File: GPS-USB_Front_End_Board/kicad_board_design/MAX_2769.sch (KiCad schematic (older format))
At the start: 50 parts, among them J3 SMA, P2 CONN_01X03, U4 MAX8510, U5 MAX8510, U6 MAX2771, U7 SAWTEK-855969, U8 LT1719S6 -- Not Populated, X1 13.368MHz TCXO

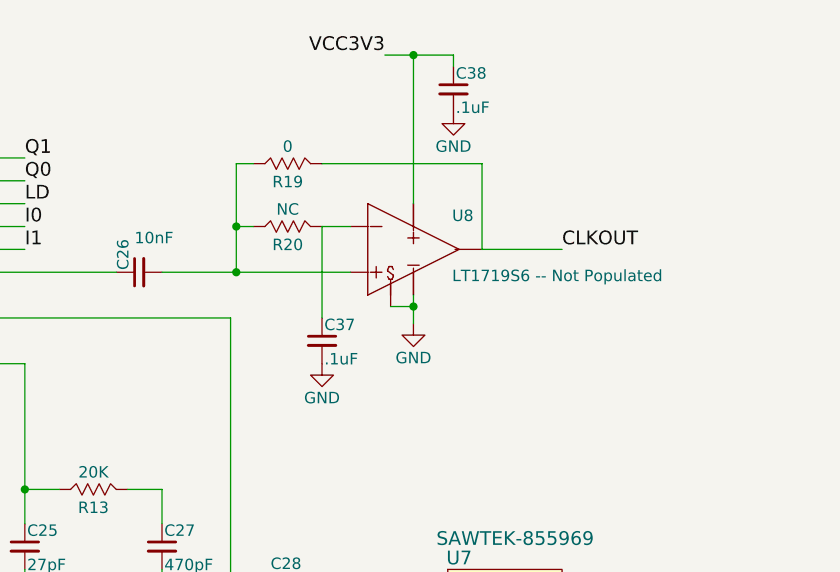
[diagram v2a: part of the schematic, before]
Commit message: Moved optional Maxim clk fix circuit to FTDI side.
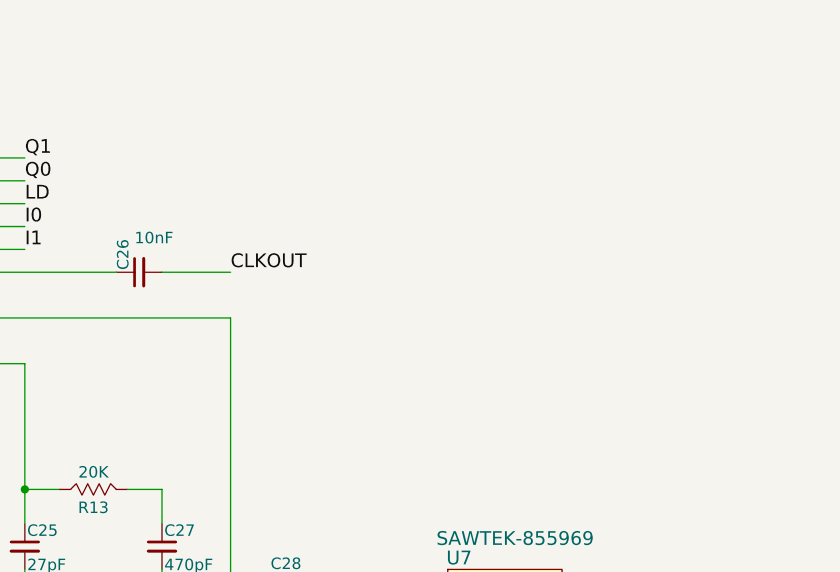
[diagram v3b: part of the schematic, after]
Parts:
- removed C37, C38: .1uF, Capacitors_SMD:C_0402, symbol C_Small
- removed R19: 0, Resistors_SMD:R_0603_HandSoldering, symbol R
- removed R20: NC, Resistors_SMD:R_0603_HandSoldering, symbol R
- removed U8: LT1719S6 -- Not Populated, rf:TSOT-23_S6, symbol LT1719S6
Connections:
- net CLKOUT: now also C26.2
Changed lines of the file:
@@
 	0    1    1    0
-$EndComp
-$Comp
-L LT1719S6 U8
-U 1 1 5B5E9B54
-P 9375 1250
-F 0 "U8" H 9544 968 50  0000 L BNN
-F 1 "LT1719S6 -- Not Populated" H 9544 705 50  0000 L BNN
-F 2 "rf:TSOT-23_S6" H 9375 1250 60  0001 C CNN
-F 3 "Unavailable" H 9375 1250 50  0001 L BNN
-F 4 "LT1719" H 9375 1250 50  0001 L BNN "Field4"
-F 5 "None" H 9375 1250 50  0001 L BNN "Field5"
-F 6 "Analog Devices / Linear Technology" H 9375 1250 50  0001 L BNN "Field6"
-F 7 "None" H 9375 1250 50  0001 L BNN "Field7"
-F 8 "Linear Tech" H 0   0   50  0001 C CNN "MFR"
-F 9 "LT1719IS6#TRMPBF" H 0   0   50  0001 C CNN "MPN"
-F 10 "Digikey" H 0   0   50  0001 C CNN "SPR"
-F 11 "LT1719IS6#TRMPBFCT-ND" H 0   0   50  0001 C CNN "SPN"
-F 12 "-" H 0   0   50  0001 C CNN "SPURL"
-	1    9375 1250
-	1    0    0    -1
-$EndComp
-$Comp
-L R R20
-U 1 1 5B5E9ED0
-P 8825 1550
-F 0 "R20" V 8905 1550 50  0000 C CNN
-F 1 "NC" V 8750 1550 50  0000 C CNN
-F 2 "Resistors_SMD:R_0603_HandSoldering" V 8680 1550 50  0001 C CNN
-F 3 "" H 8750 1550 50  0001 C CNN
-F 4 "Vishay" H 0   0   50  0001 C CNN "MFR"
-F 5 "CRCW06030000Z0EBC" H 0   0   50  0001 C CNN "MPN"
-F 6 "Digikey" H 0   0   50  0001 C CNN "SPR"
-F 7 "541-4013-1-ND" H 0   0   50  0001 C CNN "SPN"
-F 8 "-" H 0   0   50  0001 C CNN "SPURL"
-	1    8825 1550
-	0    1    1    0
-$EndComp
-$Comp
-L GND #PWR040
-U 1 1 5B5EA299
-P 8975 2150
-F 0 "#PWR040" H 8975 1900 50  0001 C CNN
-F 1 "GND" H 8975 2000 50  0000 C CNN
-F 2 "" H 8975 2150 50  0000 C CNN
-F 3 "" H 8975 2150 50  0000 C CNN
-	1    8975 2150
-	1    0    0    -1
-$EndComp
-$Comp
-L GND #PWR041
-U 1 1 5B5EAC9C
-P 9375 1975
-F 0 "#PWR041" H 9375 1725 50  0001 C CNN
-F 1 "GND" H 9375 1825 50  0000 C CNN
-F 2 "" H 9375 1975 50  0000 C CNN
-F 3 "" H 9375 1975 50  0000 C CNN
-	1    9375 1975
-	1    0    0    -1
-$EndComp
-$Comp
-L R R19
-U 1 1 5B5EB863
-P 8825 1275
-F 0 "R19" V 8905 1275 50  0000 C CNN
-F 1 "0" V 8750 1275 50  0000 C CNN
-F 2 "Resistors_SMD:R_0603_HandSoldering" V 8680 1275 50  0001 C CNN
-F 3 "" H 8750 1275 50  0001 C CNN
-F 4 "Vishay" H 0   0   50  0001 C CNN "MFR"
-F 5 "CRCW06030000Z0EBC" H 0   0   50  0001 C CNN "MPN"
-F 6 "Digikey" H 0   0   50  0001 C CNN "SPR"
-F 7 "541-4013-1-ND" H 0   0   50  0001 C CNN "SPN"
-F 8 "-" H 0   0   50  0001 C CNN "SPURL"
-	1    8825 1275
-	0    1    1    0
-$EndComp
-$Comp
-L C_Small C38
-U 1 1 5B5EE1F7
-P 9550 950
-F 0 "C38" H 9560 1020 50  0000 L CNN
-F 1 ".1uF" H 9560 870 50  0000 L CNN
-F 2 "Capacitors_SMD:C_0402" H 9550 950 50  0001 C CNN
-F 3 "" H 9550 950 50  0001 C CNN
-F 4 "TDK" H 0   0   50  0001 C CNN "MFR"
-F 5 "CGA2B1X7R1C104K050BC" H 0   0   50  0001 C CNN "MPN"
-F 6 "Digikey" H 0   0   50  0001 C CNN "SPR"
-F 7 "445-5613-1-ND" H 0   0   50  0001 C CNN "SPN"
-F 8 "-" H 0   0   50  0001 C CNN "SPURL"
-	1    9550 950
-	1    0    0    -1
-$EndComp
-$Comp
-L GND #PWR042
-U 1 1 5B5EE330
-P 9550 1050
-F 0 "#PWR042" H 9550 800 50  0001 C CNN
-F 1 "GND" H 9550 900 50  0000 C CNN
-F 2 "" H 9550 1050 50  0000 C CNN
-F 3 "" H 9550 1050 50  0000 C CNN
-	1    9550 1050
-	1    0    0    -1
 $EndComp
 Text Label 3100 2650 2    60   ~ 0
@@
 Text Label 7675 1650 0    60   ~ 0
 I1
-Text Label 10025 1650 0    60   ~ 0
+Text Label 8575 1750 0    60   ~ 0
 CLKOUT
 Text Label 2175 2650 0    60   ~ 0
@@
 Text Label 1850 1650 0    60   ~ 0
 VCC3V3
-Text Label 9250 800  2    60   ~ 0
-VCC3V3
 Text Label 1825 4375 0    60   ~ 0
 +5V
@@
 	7475 1650 7675 1650
 Wire Wire Line
-	8275 1750 9100 1750
-Wire Wire Line
 	1400 2650 1775 2650
 Wire Wire Line
@@
 Wire Wire Line
 	8575 3150 8725 3150
-Wire Wire Line
-	9100 1550 8975 1550
-Wire Wire Line
-	8675 1550 8600 1550
-Wire Wire Line
-	8600 1275 8600 1750
-Wire Wire Line
-	8975 1550 8975 1950
-Wire Wire Line
-	9375 1850 9375 1975
-Wire Wire Line
-	9275 1900 9375 1900
-Wire Wire Line
-	8600 1275 8675 1275
-Wire Wire Line
-	8975 1275 9675 1275
-Wire Wire Line
-	9675 1275 9675 1650
-Wire Wire Line
-	9675 1650 10025 1650
-Wire Wire Line
-	9250 800  9550 800
-Wire Wire Line
-	9375 800  9375 1450
-Wire Wire Line
-	9550 800  9550 850
 Wire Wire Line
 	1400 1650 1850 1650
@@
 Connection ~ 10475 5800
 Connection ~ 5625 1450
-Connection ~ 8600 1750
-Connection ~ 9375 1900
-Connection ~ 8600 1550
-Connection ~ 9375 800
 NoConn ~ 5875 3250
 NoConn ~ 4750 3150
@@
 	0    1    1    0
 $EndComp
-$Comp
-L C_Small C37
-U 1 1 5D44AA0F
-P 8975 2050
-F 0 "C37" H 8985 2120 50  0000 L CNN
-F 1 ".1uF" H 8985 1970 50  0000 L CNN
-F 2 "Capacitors_SMD:C_0402" H 8975 2050 50  0001 C CNN
-F 3 "" H 8975 2050 50  0001 C CNN
-F 4 "TDK" H 4050 150 50  0001 C CNN "MFR"
-F 5 "CGA2B1X7R1C104K050BC" H 4050 150 50  0001 C CNN "MPN"
-F 6 "Digikey" H 4050 150 50  0001 C CNN "SPR"
-F 7 "445-5613-1-ND" H 4050 150 50  0001 C CNN "SPN"
-F 8 "-" H 4050 150 50  0001 C CNN "SPURL"
-	1    8975 2050
-	1    0    0    -1
-$EndComp
+Wire Wire Line
+	8275 1750 8575 1750
 $EndSCHEMATC

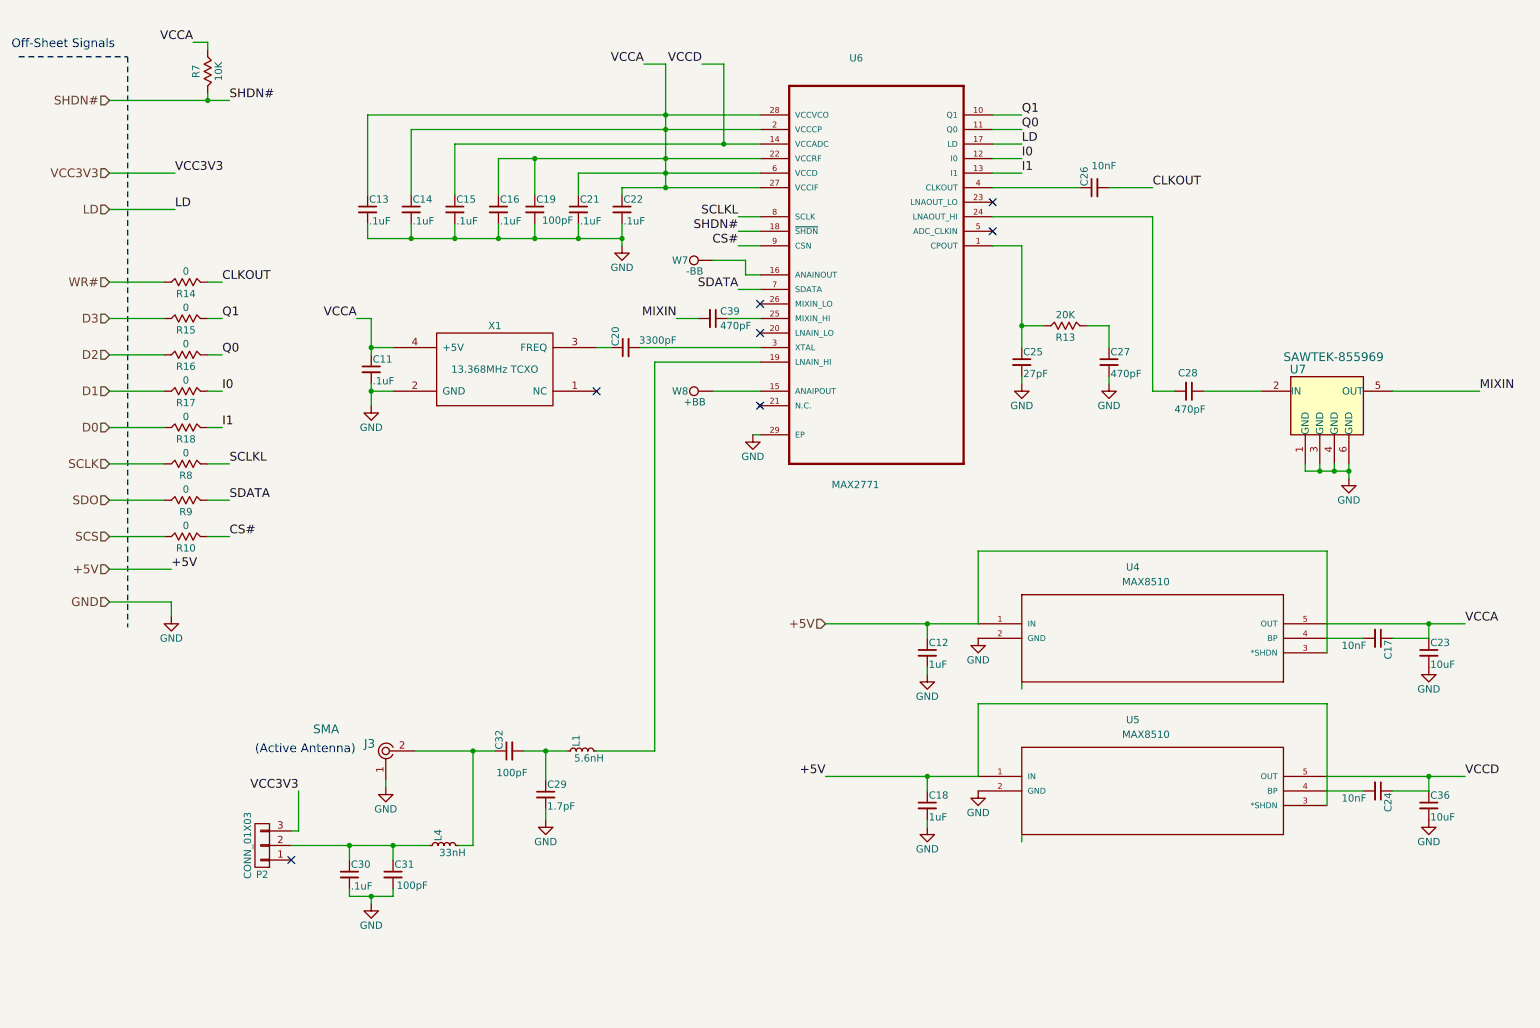
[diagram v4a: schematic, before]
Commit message: Change SMA footprint, add SAW filter, extend header pins.
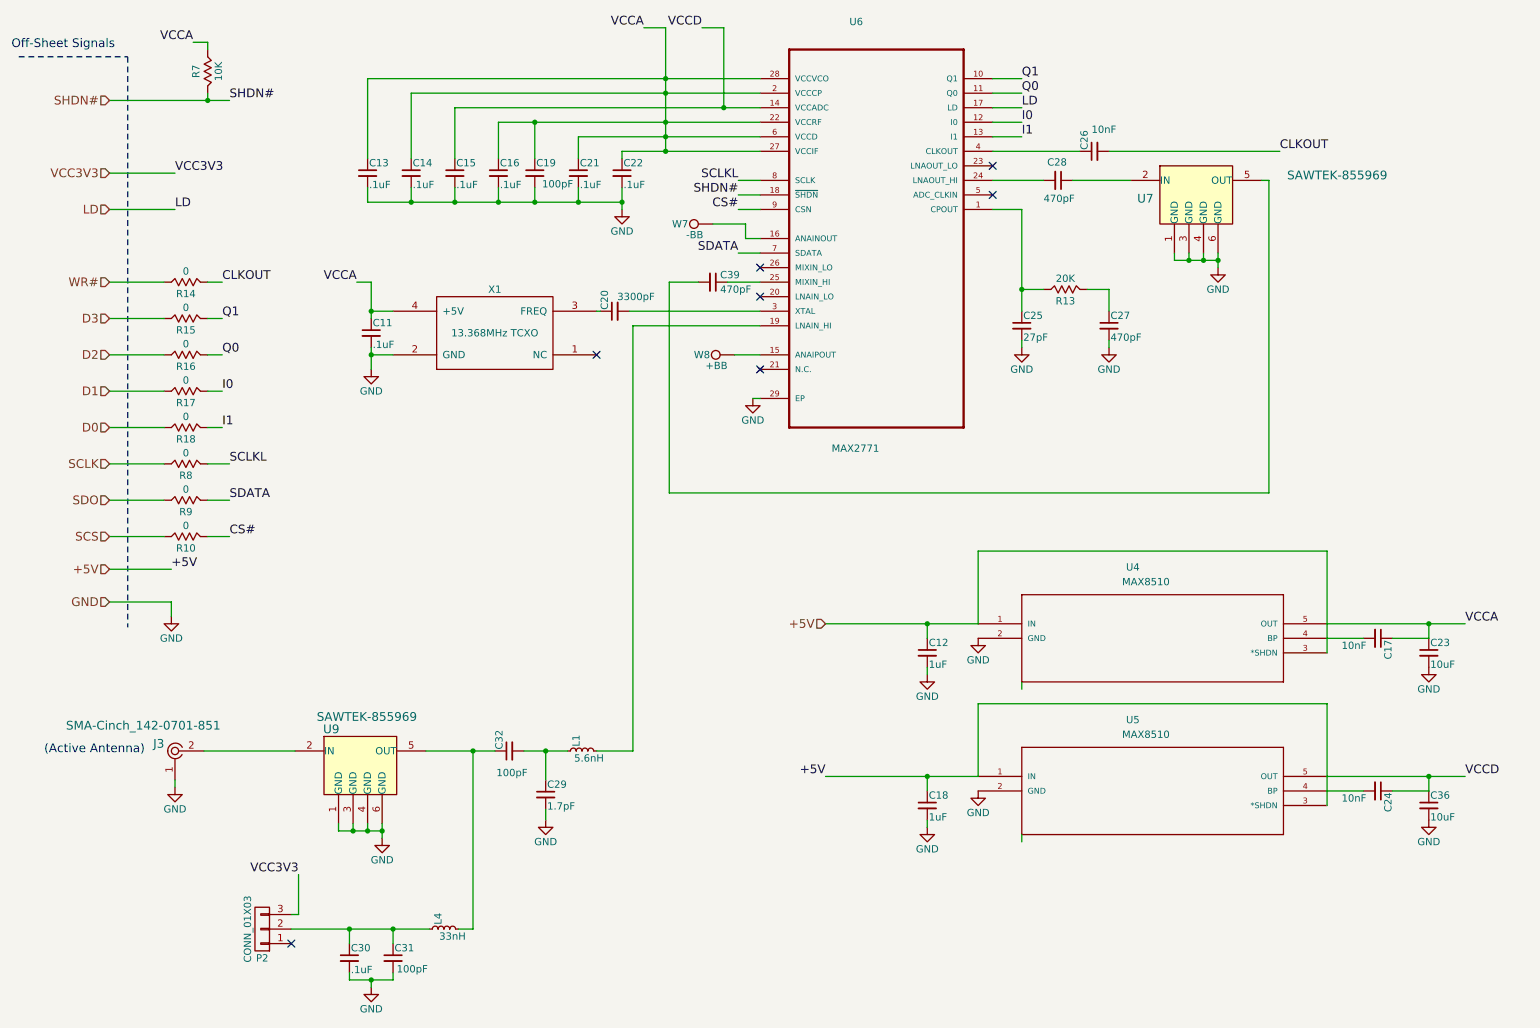
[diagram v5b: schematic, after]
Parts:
- added U9: SAWTEK-855969, rf:Sawtek_855969, symbol SAWTEK-855969
- J3: value SMA -> SMA-Cinch_142-0701-851; footprint digikey-footprints:RF_SMA_Vertical_5-1814832-1 -> rf:Cinch_142-0701-851
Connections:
- net GND: now also U9.1 (GND), U9.3 (GND), U9.4 (GND), U9.6 (GND)
- net at C32.1, L4.2: now also U9.5 (OUT); no longer J3.2
- net MIXIN: no longer names the net of C39.2, U7.5 (OUT)
- new net: J3.2, U9.2 (IN)
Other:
- moved on the sheet: C11, C13, C14, C15, C16, C19, C20, C21, C22, C25, C26, C27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

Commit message: Add signals to header.
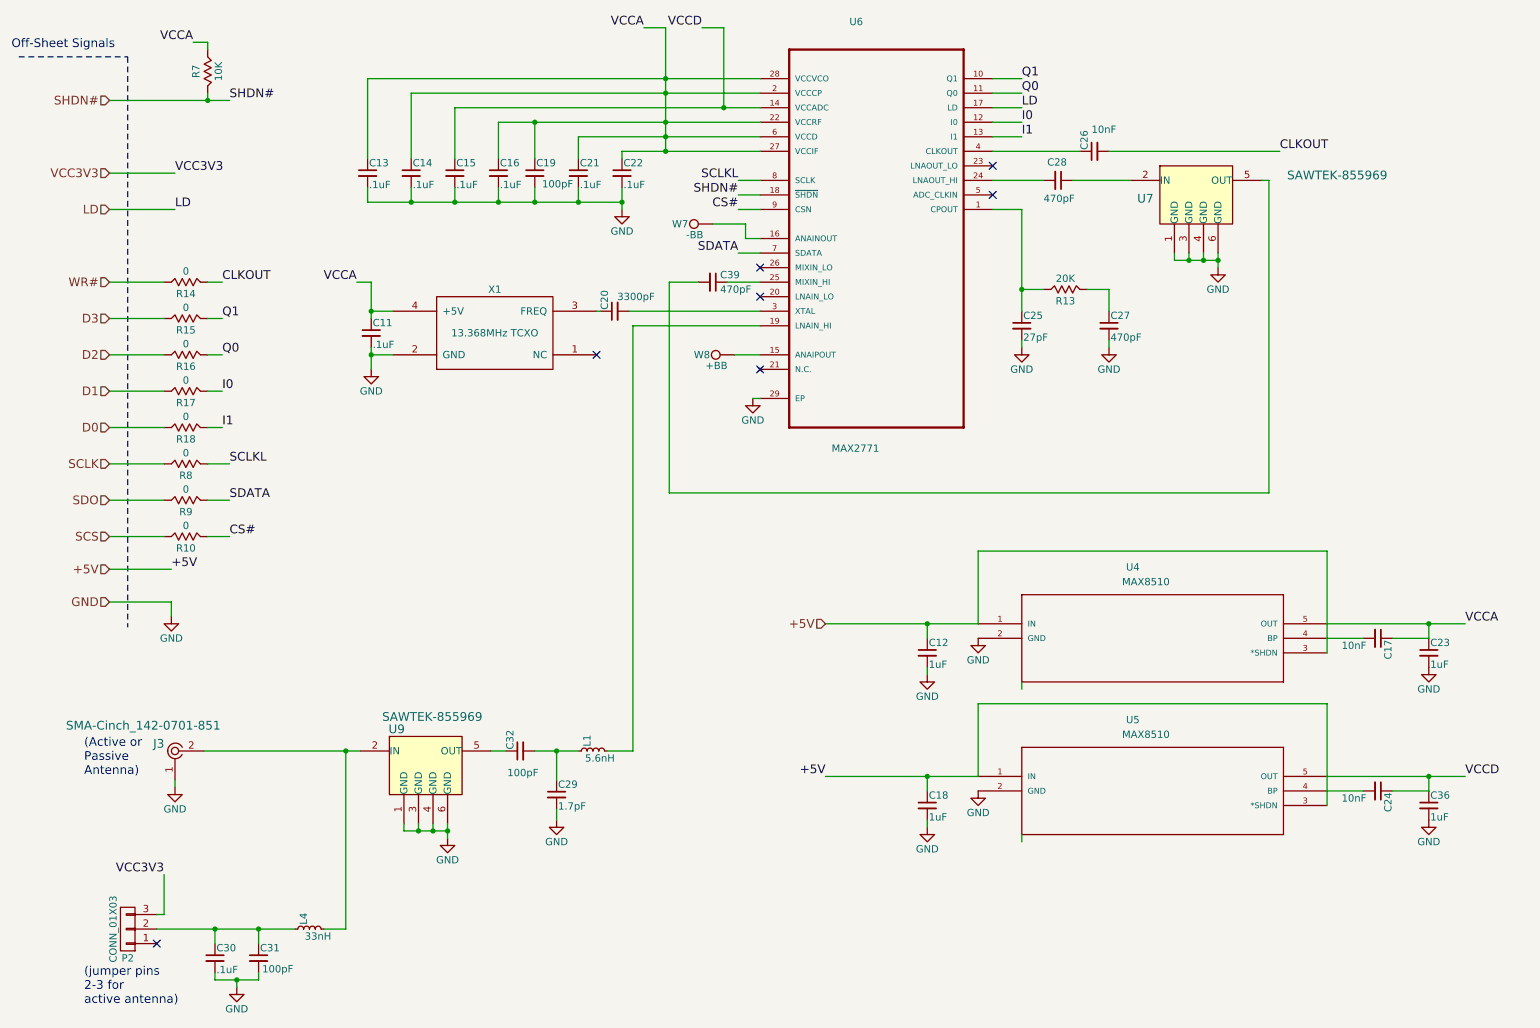
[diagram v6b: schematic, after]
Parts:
- C23, C36: value 10uF -> 1uF; MFR Samsung -> Kemet; MPN CL21A106KPFNNNG -> C0805C105K4RACTU; SPN 1276-6456-1-ND -> 399-1284-1-ND
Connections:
- net at J3.2, U9.2 (IN): now also L4.2
- net at C32.1, U9.5 (OUT): no longer L4.2
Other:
- note added: "(Active or\nPassive \nAntenna)"
- note added: "(jumper pins \n2-3 for \nactive antenna)"
- note removed: "(Active Antenna)"
- moved on the sheet: C29, C30, C31, C32, L1, L4, P2, U9

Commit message: Add LED P/N.  Process BOM prior to order.
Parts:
- P2, U6: SPURL (none) -> -
